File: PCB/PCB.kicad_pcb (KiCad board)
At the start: 2 copper layers, 120.6 x 120.6 mm, 11 parts

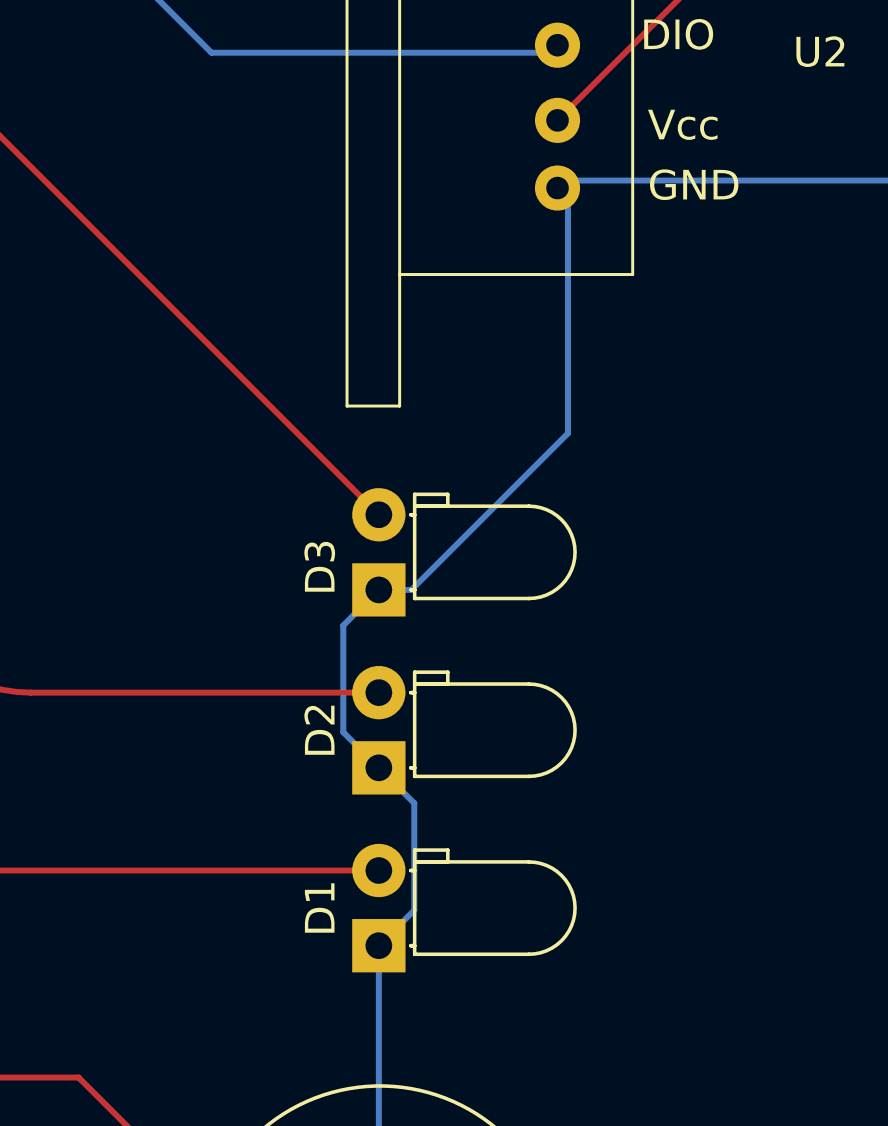
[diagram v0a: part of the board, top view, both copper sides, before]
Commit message: Created git-ignore file
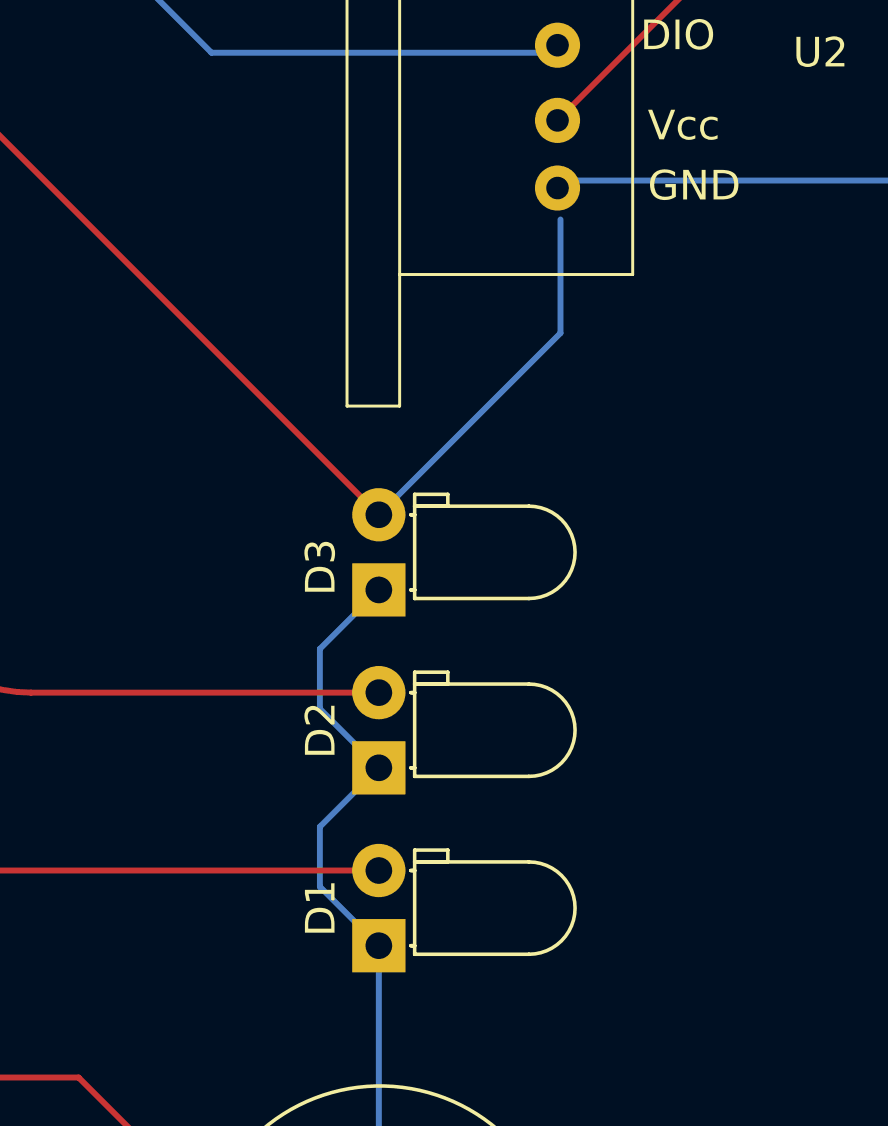
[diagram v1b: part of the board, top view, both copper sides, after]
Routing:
- net GND: track 204.0 -> 188.0 mm
- net Net-(D3-A): track 29.6 -> 42.1 mm
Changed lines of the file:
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@@
 	)
 	(segment
-		(start 164.481 126.082)
+		(start 161.29 126.873)
 		(end 163.281 124.882)
+		(width 0.2)
+		(layer "B.Cu")
+		(net 2)
+	)
+	(segment
+		(start 183.602 61.428)
+		(end 163.19 61.428)
 		(width 0.2)
 		(layer "B.Cu")
@@
 	)
 	(segment
-		(start 163.281 124.882)
-		(end 162.081 123.682)
-		(width 0.2)
-		(layer "B.Cu")
-		(net 2)
-	)
-	(segment
-		(start 163.281 118.872)
-		(end 164.381 118.872)
+		(start 194.31 97.282)
+		(end 194.31 72.136)
 		(width 0.2)
 		(layer "B.Cu")
@@
 	)
 	(segment
+		(start 161.29 122.891)
+		(end 161.29 120.863)
+		(width 0.2)
+		(layer "B.Cu")
+		(net 2)
+	)
+	(segment
+		(start 133.858 38.354)
+		(end 132.01 40.202)
+		(width 0.2)
+		(layer "B.Cu")
+		(net 2)
+	)
+	(segment
+		(start 186.552 105.04)
+		(end 194.31 97.282)
+		(width 0.2)
+		(layer "B.Cu")
+		(net 2)
+	)
+	(segment
+		(start 163.19 38.354)
+		(end 133.858 38.354)
+		(width 0.2)
+		(layer "B.Cu")
+		(net 2)
+	)
+	(segment
 		(start 163.281 130.892)
-		(end 164.481 129.692)
+		(end 161.29 128.901)
+		(width 0.2)
+		(layer "B.Cu")
+		(net 2)
+	)
+	(segment
+		(start 161.29 128.901)
+		(end 161.29 126.873)
+		(width 0.2)
+		(layer "B.Cu")
+		(net 2)
+	)
+	(segment
+		(start 163.281 124.882)
+		(end 161.29 122.891)
+		(width 0.2)
+		(layer "B.Cu")
+		(net 2)
+	)
+	(segment
+		(start 163.19 61.428)
+		(end 163.19 38.354)
+		(width 0.2)
+		(layer "B.Cu")
+		(net 2)
+	)
+	(segment
+		(start 161.29 120.863)
+		(end 163.281 118.872)
+		(width 0.2)
+		(layer "B.Cu")
+		(net 2)
+	)
+	(segment
+		(start 163.281 137.891)
+		(end 163.281 130.892)
+		(width 0.2)
+		(layer "B.Cu")
+		(net 2)
+	)
+	(segment
+		(start 132.01 54.784)
+		(end 133.26 56.034)
 		(width 0.2)
 		(layer "B.Cu")
@@
 	)
 	(segment
-		(start 133.858 38.354)
-		(end 132.01 40.202)
-		(width 0.2)
-		(layer "B.Cu")
-		(net 2)
-	)
-	(segment
 		(start 194.31 72.136)
 		(end 183.602 61.428)
-		(width 0.2)
-		(layer "B.Cu")
-		(net 2)
-	)
-	(segment
-		(start 163.19 38.354)
-		(end 133.858 38.354)
-		(width 0.2)
-		(layer "B.Cu")
-		(net 2)
-	)
-	(segment
-		(start 162.081 123.682)
-		(end 162.081 120.072)
-		(width 0.2)
-		(layer "B.Cu")
-		(net 2)
-	)
-	(segment
-		(start 163.19 61.428)
-		(end 163.19 38.354)
-		(width 0.2)
-		(layer "B.Cu")
-		(net 2)
-	)
-	(segment
-		(start 169.672 113.581)
-		(end 169.672 105.394)
-		(width 0.2)
-		(layer "B.Cu")
-		(net 2)
-	)
-	(segment
-		(start 163.281 137.891)
-		(end 163.281 130.892)
-		(width 0.2)
-		(layer "B.Cu")
-		(net 2)
-	)
-	(segment
-		(start 132.01 54.784)
-		(end 133.26 56.034)
-		(width 0.2)
-		(layer "B.Cu")
-		(net 2)
-	)
-	(segment
-		(start 162.081 120.072)
-		(end 163.281 118.872)
-		(width 0.2)
-		(layer "B.Cu")
-		(net 2)
-	)
-	(segment
-		(start 169.672 105.394)
-		(end 169.318 105.04)
-		(width 0.2)
-		(layer "B.Cu")
-		(net 2)
-	)
-	(segment
-		(start 164.381 118.872)
-		(end 169.672 113.581)
-		(width 0.2)
-		(layer "B.Cu")
-		(net 2)
-	)
-	(segment
-		(start 186.552 105.04)
-		(end 194.31 97.282)
-		(width 0.2)
-		(layer "B.Cu")
-		(net 2)
-	)
-	(segment
-		(start 194.31 97.282)
-		(end 194.31 72.136)
-		(width 0.2)
-		(layer "B.Cu")
-		(net 2)
-	)
-	(segment
-		(start 164.481 129.692)
-		(end 164.481 126.082)
-		(width 0.2)
-		(layer "B.Cu")
-		(net 2)
-	)
-	(segment
-		(start 183.602 61.428)
-		(end 163.19 61.428)
 		(width 0.2)
 		(layer "B.Cu")
@@
 		(width 0.5)
 		(layer "F.Cu")
+		(net 5)
+	)
+	(segment
+		(start 169.418 110.195)
+		(end 169.418 106.356)
+		(width 0.2)
+		(layer "B.Cu")
+		(net 5)
+	)
+	(segment
+		(start 163.281 116.332)
+		(end 169.418 110.195)
+		(width 0.2)
+		(layer "B.Cu")
 		(net 5)
 	)
@@
 			(thermal_gap 0.5)
 			(thermal_bridge_width 0.5)
+			(island_removal_mode 1)
+			(island_area_min 10)
 		)
 		(polygon
